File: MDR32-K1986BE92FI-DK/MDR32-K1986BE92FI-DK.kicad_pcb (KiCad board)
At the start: 2 copper layers, 57 parts, among them J1 Conn_PROBE, J2 PIN_A, J3 SYS_A, J4 USB_C_Receptacle_USB2.0_16P, J5 PIN_B, J6 SYS_B, Q1 AO3401A, SW1 IT-1181, SW2 SW_DIP_x02, SW3 IT-1181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

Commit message: start pcb sizes
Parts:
- moved J2 92.0 mm to (108.1, 47.5), turned to -90 degrees
- moved BT1 79.3 mm to (88.3, 95.2)
- moved C1 79.3 mm to (80.4, 105.0)
- moved C2 79.3 mm to (80.4, 108.0)
- moved C3 79.3 mm to (96.5, 105.1)
- moved D2 79.3 mm to (77.1, 115.2)
- moved D3 79.3 mm to (89.3, 131.3)
- moved D5 79.3 mm to (89.3, 134.4)
- moved F1 79.3 mm to (68.1, 88.2)
- moved F2 79.3 mm to (68.1, 90.7)
- moved J1 79.3 mm to (95.9, 121.8)
- moved J4 79.3 mm to (88.5, 114.8)
- moved JP1 79.3 mm to (84.9, 131.6)
- moved JP2 79.3 mm to (84.9, 135.1)
- moved R1 79.3 mm to (68.1, 93.2)
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
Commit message: change pinout on header
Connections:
- J2 pad 1: /PA0 -> GND
- J2 pad 10: /PB9 -> /PA6
- J2 pad 11: /PB8 -> /PA5
- J2 pad 12: /PB7 -> /PA4
- J2 pad 13: /PB6 -> /PA3
- J2 pad 14: /PB5 -> /PA2
- J2 pad 15: GND -> /PA1
- J2 pad 16: GND -> /PA0
- J2 pad 2: /PA1 -> GND
- J2 pad 3: /PA2 -> /PB5
- J2 pad 4: /PA3 -> /PB6
- J2 pad 5: /PA4 -> /PB7
- J2 pad 6: /PA5 -> /PB8
- J2 pad 7: /PA6 -> /PB9
- J2 pad 8: /PA7 -> /PB10
- J2 pad 9: /PB10 -> /PA7
- J3 pad 1: /JATDO -> GND
- J3 pad 10: GND -> /JATDO
- J3 pad 2: /JATMS -> +3V3_SRC
- J3 pad 3: /JATCK -> +BATT_SRC
- J3 pad 4: /JATDI -> /WAKEUP
- J3 pad 5: /JAnTRS -> /nRESET
- J3 pad 6: /nRESET -> /JAnTRS
- J3 pad 7: +BATT_SRC -> /JATDI
- J3 pad 8: +3V3_SRC -> /JATCK
- J3 pad 9: VUSB -> /JATMS
- J5 pad 1: /PC0 -> /PF0
- J5 pad 10: /PE3 -> /PE0
- J5 pad 11: /PE6 -> /PD7
- J5 pad 12: /PE7 -> /PD6
- J5 pad 13: /PF3 -> /PD5
- J5 pad 14: /PF2 -> /PC2
- J5 pad 15: /PF1 -> /PC1
- J5 pad 16: /PF0 -> /PC0
- J5 pad 2: /PC1 -> /PF1
- J5 pad 3: /PC2 -> /PF2
- J5 pad 4: /PD5 -> /PF3
- J5 pad 5: /PD6 -> /PE7
- J5 pad 6: /PD7 -> /PE6
- J5 pad 7: /PE0 -> /PE3
- J5 pad 8: /PE1 -> /PE2
- J5 pad 9: /PE2 -> /PE1
- J6 pad 1: /WAKEUP -> GND
- J6 pad 10: GND -> /JBTDO
- J6 pad 2: /JBTDO -> VUSB
- J6 pad 3: /JBTMS -> /PF4_MODE0
- J6 pad 4: /JBTCK -> /PF5_MODE1
- J6 pad 5: /JBTDI -> /PF6_MODE2
- J6 pad 7: /PF6_MODE2 -> /JBTDI
- J6 pad 8: /PF5_MODE1 -> /JBTCK
- J6 pad 9: /PF4_MODE0 -> /JBTMS
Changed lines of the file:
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@@
 		)
 		(fp_text user "${REFERENCE}"
-			(at 0 19.05 360)
+			(at 0 19.05 0)
 			(layer "F.Fab")
 			(effects
@@
 			(layers "*.Cu" "*.Mask")
 			(remove_unused_layers no)
-			(net 36 "/PC0")
+			(net 62 "/PF0")
 			(pinfunction "Pin_1")
 			(pintype "passive")
@@
 			(layers "*.Cu" "*.Mask")
 			(remove_unused_layers no)
-			(net 58 "/PC1")
+			(net 39 "/PF1")
 			(pinfunction "Pin_2")
 			(pintype "passive")
@@
 			(layers "*.Cu" "*.Mask")
 			(remove_unused_layers no)
-			(net 20 "/PC2")
+			(net 33 "/PF2")
 			(pinfunction "Pin_3")
 			(pintype "passive")
@@
 			(layers "*.Cu" "*.Mask")
 			(remove_unused_layers no)
-			(net 19 "/PD5")
+			(net 45 "/PF3")
 			(pinfunction "Pin_4")
 			(pintype "passive")
@@
 			(layers "*.Cu" "*.Mask")
 			(remove_unused_layers no)
-			(net 38 "/PD6")
+			(net 66 "/PE7")
 			(pinfunction "Pin_5")
 			(pintype "passive")
@@
 			(layers "*.Cu" "*.Mask")
 			(remove_unused_layers no)
-			(net 43 "/PD7")
+			(net 67 "/PE6")
 			(pinfunction "Pin_6")
 			(pintype "passive")
@@
 			(layers "*.Cu" "*.Mask")
 			(remove_unused_layers no)
-			(net 47 "/PE0")
+			(net 44 "/PE3")
 			(pinfunction "Pin_7")
 			(pintype "passive")
@@
 			(layers "*.Cu" "*.Mask")
 			(remove_unused_layers no)
-			(net 48 "/PE1")
+			(net 61 "/PE2")
 			(pinfunction "Pin_8")
 			(pintype "passive")
@@
 			(layers "*.Cu" "*.Mask")
 			(remove_unused_layers no)
-			(net 61 "/PE2")
+			(net 48 "/PE1")
 			(pinfunction "Pin_9")
 			(pintype "passive")
@@
 			(layers "*.Cu" "*.Mask")
 			(remove_unused_layers no)
-			(net 44 "/PE3")
+			(net 47 "/PE0")
 			(pinfunction "Pin_10")
 			(pintype "passive")
@@
 			(layers "*.Cu" "*.Mask")
 			(remove_unused_layers no)
-			(net 67 "/PE6")
+			(net 43 "/PD7")
 			(pinfunction "Pin_11")
 			(pintype "passive")
@@
 			(layers "*.Cu" "*.Mask")
 			(remove_unused_layers no)
-			(net 66 "/PE7")
+			(net 38 "/PD6")
 			(pinfunction "Pin_12")
 			(pintype "passive")
@@
 			(layers "*.Cu" "*.Mask")
 			(remove_unused_layers no)
-			(net 45 "/PF3")
+			(net 19 "/PD5")
 			(pinfunction "Pin_13")
 			(pintype "passive")
@@
 			(layers "*.Cu" "*.Mask")
 			(remove_unused_layers no)
-			(net 33 "/PF2")
+			(net 20 "/PC2")
 			(pinfunction "Pin_14")
 			(pintype "passive")
@@
 			(layers "*.Cu" "*.Mask")
 			(remove_unused_layers no)
-			(net 39 "/PF1")
+			(net 58 "/PC1")
 			(pinfunction "Pin_15")
 			(pintype "passive")
@@
 			(layers "*.Cu" "*.Mask")
 			(remove_unused_layers no)
-			(net 62 "/PF0")
+			(net 36 "/PC0")
 			(pinfunction "Pin_16")
 			(pintype "passive")
@@
 		)
 		(fp_text user "${REFERENCE}"
-			(at 0 11.43 360)
+			(at 0 11.43 0)
 			(layer "F.Fab")
 			(effects
@@
 			(layers "*.Cu" "*.Mask")
 			(remove_unused_layers no)
-			(net 8 "/WAKEUP")
+			(net 9 "GND")
 			(pinfunction "Pin_1")
 			(pintype "passive")
@@
 			(layers "*.Cu" "*.Mask")
 			(remove_unused_layers no)
-			(net 6 "/JBTDO")
+			(net 31 "VUSB")
 			(pinfunction "Pin_2")
 			(pintype "passive")
@@
 			(layers "*.Cu" "*.Mask")
 			(remove_unused_layers no)
-			(net 4 "/JBTMS")
+			(net 16 "/PF4_MODE0")
 			(pinfunction "Pin_3")
 			(pintype "passive")
@@
 			(layers "*.Cu" "*.Mask")
 			(remove_unused_layers no)
-			(net 5 "/JBTCK")
+			(net 17 "/PF5_MODE1")
 			(pinfunction "Pin_4")
 			(pintype "passive")
@@
 			(layers "*.Cu" "*.Mask")
 			(remove_unused_layers no)
-			(net 3 "/JBTDI")
+			(net 18 "/PF6_MODE2")
 			(pinfunction "Pin_5")
 			(pintype "passive")
@@
 			(layers "*.Cu" "*.Mask")
 			(remove_unused_layers no)
-			(net 18 "/PF6_MODE2")
+			(net 3 "/JBTDI")
 			(pinfunction "Pin_7")
 			(pintype "passive")
@@
 			(layers "*.Cu" "*.Mask")
 			(remove_unused_layers no)
-			(net 17 "/PF5_MODE1")
+			(net 5 "/JBTCK")
 			(pinfunction "Pin_8")
 			(pintype "passive")
@@
 			(layers "*.Cu" "*.Mask")
 			(remove_unused_layers no)
-			(net 16 "/PF4_MODE0")
+			(net 4 "/JBTMS")
 			(pinfunction "Pin_9")
 			(pintype "passive")
@@
 			(layers "*.Cu" "*.Mask")
 			(remove_unused_layers no)
-			(net 9 "GND")
+			(net 6 "/JBTDO")
 			(pinfunction "Pin_10")
 			(pintype "passive")
@@
 		)
 		(fp_text user "${REFERENCE}"
-			(at 0 19.05 360)
+			(at 0 19.05 0)
 			(layer "F.Fab")
 			(effects
@@
 			(layers "*.Cu" "*.Mask")
 			(remove_unused_layers no)
-			(net 60 "/PA0")
+			(net 9 "GND")
 			(pinfunction "Pin_1")
 			(pintype "passive")
@@
 			(layers "*.Cu" "*.Mask")
 			(remove_unused_layers no)
-			(net 52 "/PA1")
+			(net 9 "GND")
 			(pinfunction "Pin_2")
 			(pintype "passive")
@@
 			(layers "*.Cu" "*.Mask")
 			(remove_unused_layers no)
-			(net 35 "/PA2")
+			(net 59 "/PB5")
 			(pinfunction "Pin_3")
 			(pintype "passive")
@@
 			(layers "*.Cu" "*.Mask")
 			(remove_unused_layers no)
-			(net 37 "/PA3")
+			(net 63 "/PB6")
 			(pinfunction "Pin_4")
 			(pintype "passive")
@@
 			(layers "*.Cu" "*.Mask")
 			(remove_unused_layers no)
-			(net 46 "/PA4")
+			(net 55 "/PB7")
 			(pinfunction "Pin_5")
 			(pintype "passive")
@@
 			(layers "*.Cu" "*.Mask")
 			(remove_unused_layers no)
-			(net 56 "/PA5")
+			(net 41 "/PB8")
 			(pinfunction "Pin_6")
 			(pintype "passive")
@@
 			(layers "*.Cu" "*.Mask")
 			(remove_unused_layers no)
-			(net 53 "/PA6")
+			(net 57 "/PB9")
 			(pinfunction "Pin_7")
 			(pintype "passive")
@@
 			(layers "*.Cu" "*.Mask")
 			(remove_unused_layers no)
-			(net 49 "/PA7")
+			(net 40 "/PB10")
 			(pinfunction "Pin_8")
 			(pintype "passive")
@@
 			(layers "*.Cu" "*.Mask")
 			(remove_unused_layers no)
-			(net 40 "/PB10")
+			(net 49 "/PA7")
 			(pinfunction "Pin_9")
 			(pintype "passive")
@@
 			(layers "*.Cu" "*.Mask")
 			(remove_unused_layers no)
-			(net 57 "/PB9")
+			(net 53 "/PA6")
 			(pinfunction "Pin_10")
 			(pintype "passive")
@@
 			(layers "*.Cu" "*.Mask")
 			(remove_unused_layers no)
-			(net 41 "/PB8")
+			(net 56 "/PA5")
 			(pinfunction "Pin_11")
 			(pintype "passive")
@@
 			(layers "*.Cu" "*.Mask")
 			(remove_unused_layers no)
-			(net 55 "/PB7")
+			(net 46 "/PA4")
 			(pinfunction "Pin_12")
 			(pintype "passive")
@@
 			(layers "*.Cu" "*.Mask")
 			(remove_unused_layers no)
-			(net 63 "/PB6")
+			(net 37 "/PA3")
 			(pinfunction "Pin_13")
 			(pintype "passive")
@@
 			(layers "*.Cu" "*.Mask")
 			(remove_unused_layers no)
-			(net 59 "/PB5")
+			(net 35 "/PA2")
 			(pinfunction "Pin_14")
 			(pintype "passive")
@@
 			(layers "*.Cu" "*.Mask")
 			(remove_unused_layers no)
-			(net 9 "GND")
+			(net 52 "/PA1")
 			(pinfunction "Pin_15")
 			(pintype "passive")
@@
 			(layers "*.Cu" "*.Mask")
 			(remove_unused_layers no)
-			(net 9 "GND")
+			(net 60 "/PA0")
 			(pinfunction "Pin_16")
 			(pintype "passive")
@@
 		)
 		(fp_text user "${REFERENCE}"
-			(at 0 11.43 360)
+			(at 0 11.43 0)
 			(layer "F.Fab")
 			(effects
@@
 			(layers "*.Cu" "*.Mask")
 			(remove_unused_layers no)
-			(net 25 "/JATDO")
+			(net 9 "GND")
 			(pinfunction "Pin_1")
 			(pintype "passive")
@@
 			(layers "*.Cu" "*.Mask")
 			(remove_unused_layers no)
-			(net 13 "/JATMS")
+			(net 29 "+3V3_SRC")
 			(pinfunction "Pin_2")
 			(pintype "passive")
@@
 			(layers "*.Cu" "*.Mask")
 			(remove_unused_layers no)
-			(net 14 "/JATCK")
+			(net 27 "+BATT_SRC")
 			(pinfunction "Pin_3")
 			(pintype "passive")
@@
 			(layers "*.Cu" "*.Mask")
 			(remove_unused_layers no)
-			(net 12 "/JATDI")
+			(net 8 "/WAKEUP")
 			(pinfunction "Pin_4")
 			(pintype "passive")
@@
 			(layers "*.Cu" "*.Mask")
 			(remove_unused_layers no)
-			(net 2 "/JAnTRS")
+			(net 15 "/nRESET")
 			(pinfunction "Pin_5")
 			(pintype "passive")
@@
 			(layers "*.Cu" "*.Mask")
 			(remove_unused_layers no)
-			(net 15 "/nRESET")
+			(net 2 "/JAnTRS")
 			(pinfunction "Pin_6")
 			(pintype "passive")
@@
 			(layers "*.Cu" "*.Mask")
 			(remove_unused_layers no)
-			(net 27 "+BATT_SRC")
+			(net 12 "/JATDI")
 			(pinfunction "Pin_7")
 			(pintype "passive")
@@
 			(layers "*.Cu" "*.Mask")
 			(remove_unused_layers no)
-			(net 29 "+3V3_SRC")
+			(net 14 "/JATCK")
 			(pinfunction "Pin_8")
 			(pintype "passive")
@@
 			(layers "*.Cu" "*.Mask")
 			(remove_unused_layers no)
-			(net 31 "VUSB")
+			(net 13 "/JATMS")
 			(pinfunction "Pin_9")
 			(pintype "passive")
@@
 			(layers "*.Cu" "*.Mask")
 			(remove_unused_layers no)
-			(net 9 "GND")
+			(net 25 "/JATDO")
 			(pinfunction "Pin_10")
 			(pintype "passive")

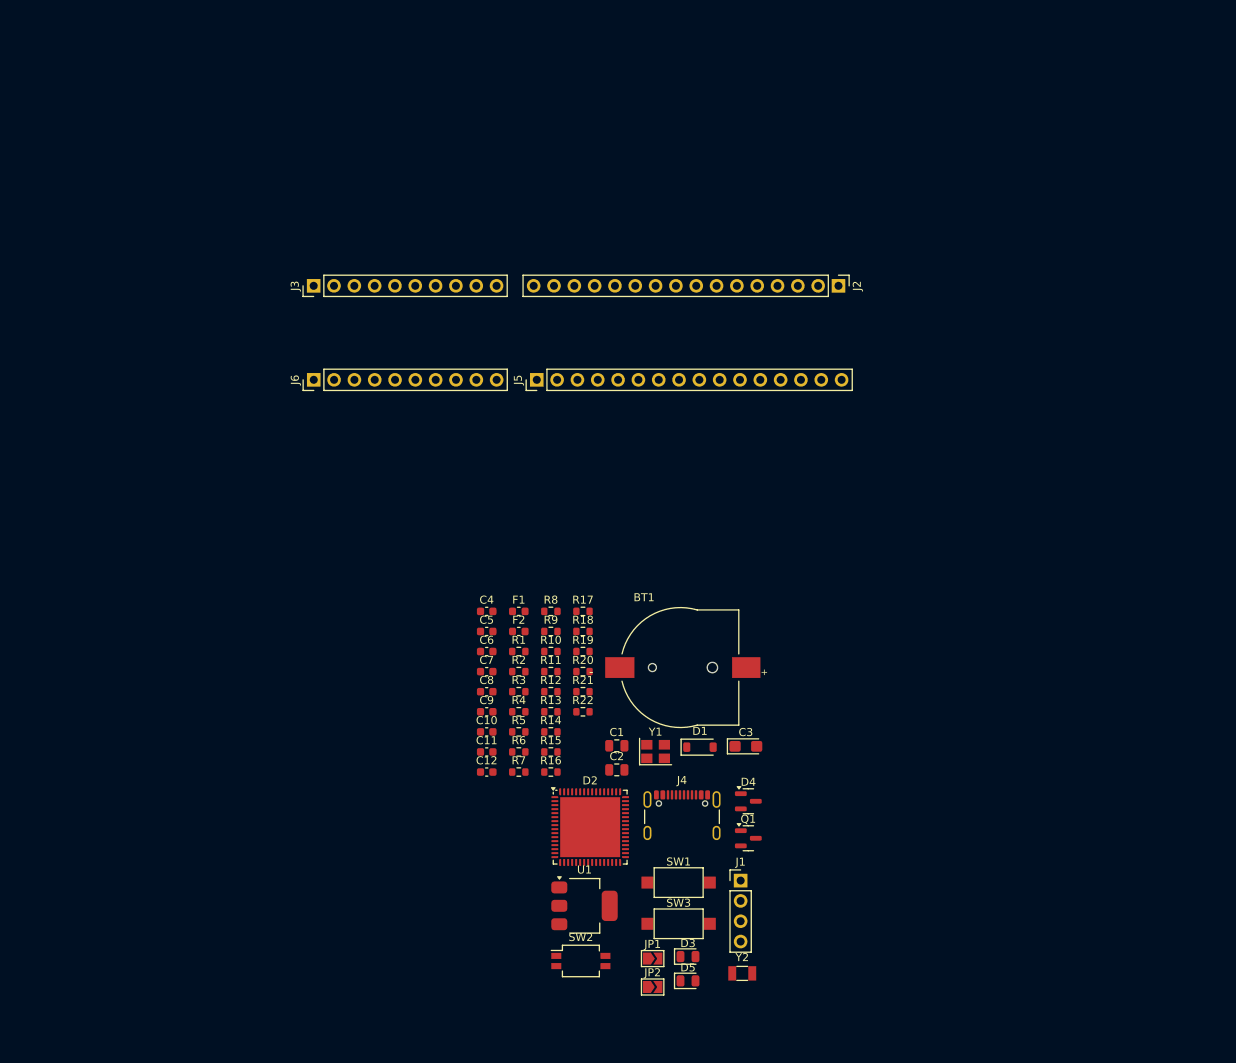
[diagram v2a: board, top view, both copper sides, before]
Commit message: position and sizes
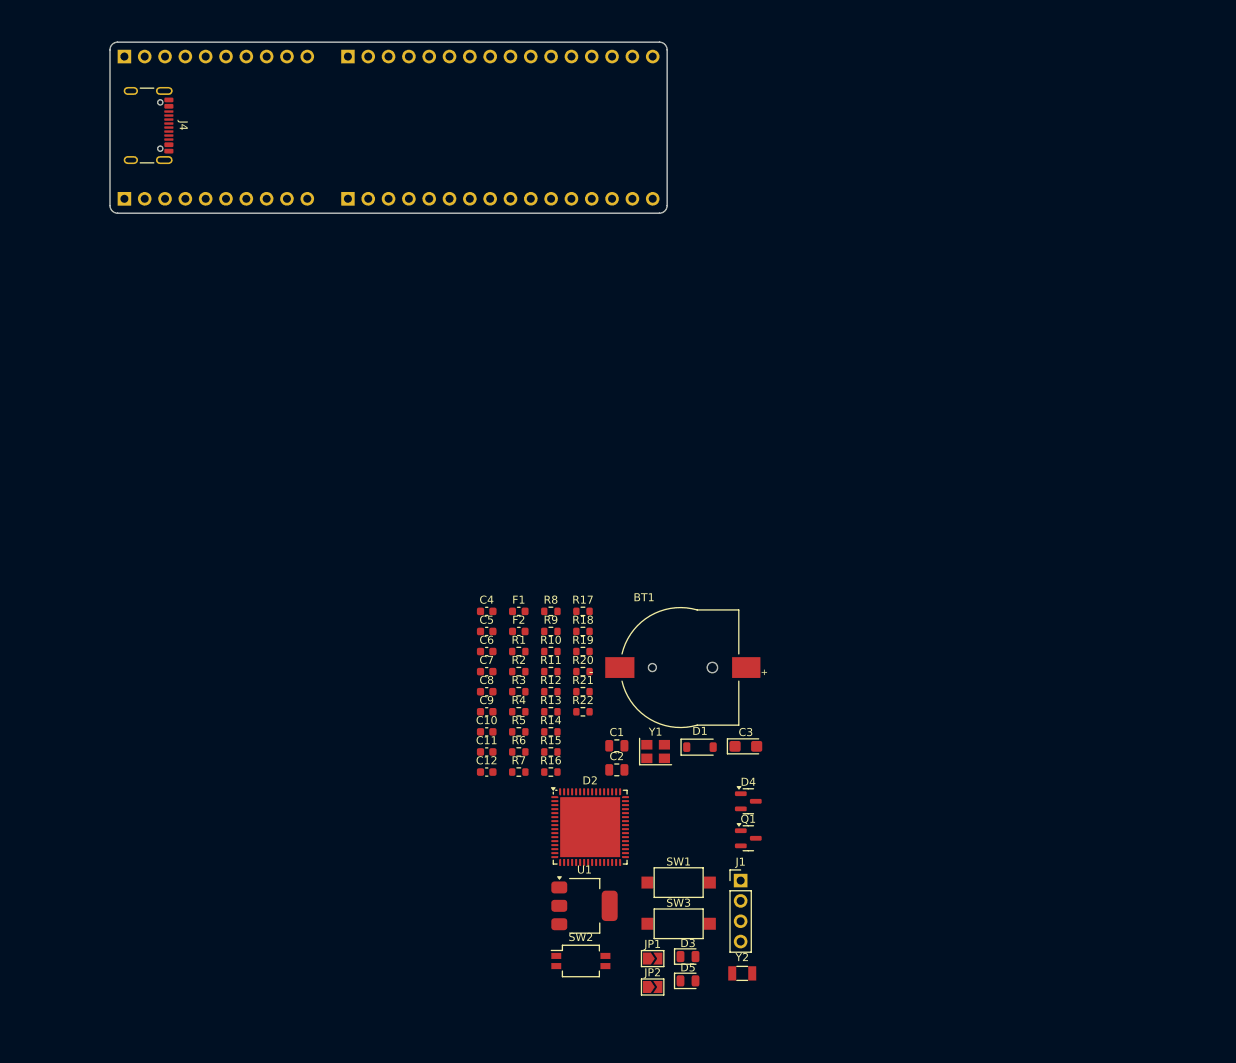
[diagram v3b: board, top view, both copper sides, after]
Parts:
- J2, J3, J5, J6: moved to B.Cu
- moved J4 110.6 mm to (20.7, 27.5), turned to -90 degrees
- moved J2 62.3 mm to (46.8, 36.6)
- moved J6 46.8 mm to (18.8, 18.8), turned to -90 degrees
- moved J5 46.8 mm to (46.8, 18.8), turned to -90 degrees
- moved J3 26.0 mm to (18.8, 36.6), turned to -90 degrees
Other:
- board outline added: 69.6 x 21.4 mm

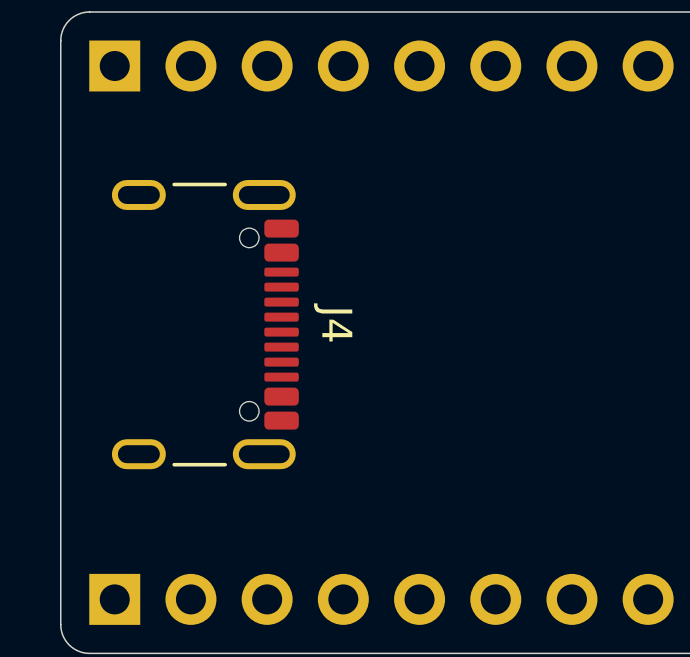
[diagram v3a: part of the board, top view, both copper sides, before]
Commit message: usb position on pcb
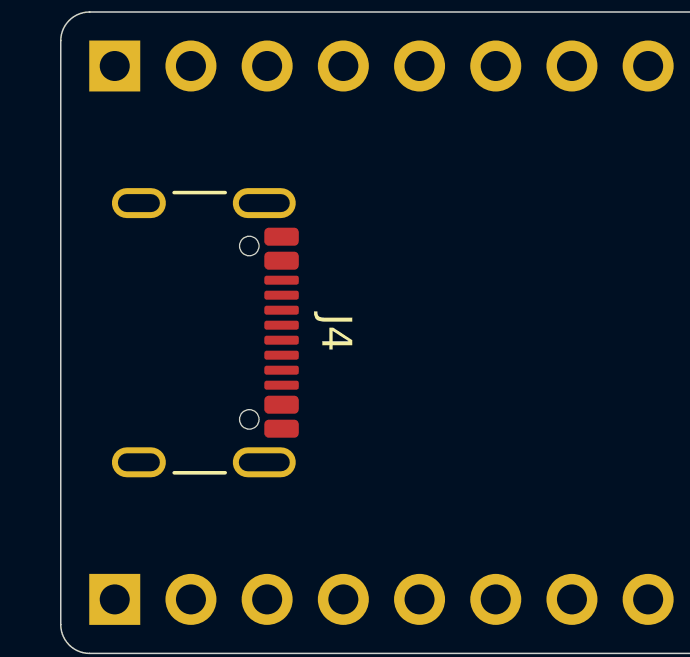
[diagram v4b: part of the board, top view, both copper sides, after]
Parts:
- moved J4 0.27 mm to (20.7, 27.7)
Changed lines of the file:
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@@
 	)
 	(footprint "Connector_USB:USB_C_Receptacle_GCT_USB4105-xx-A_16P_TopMnt_Horizontal"
+		(locked yes)
 		(layer "F.Cu")
-		(at 20.72 27.46 -90)
+		(at 20.72 27.73 -90)
 		(descr "USB 2.0 Type C Receptacle, GCT, 16P, top mounted, horizontal, 5A: https://gct.co/files/drawings/usb4105.pdf")
 		(tags "USB C Type-C Receptacle SMD USB 2.0 16P 16C USB4105-15-A USB4105-15-A-060 USB4105-15-A-120 USB4105-GF-A USB4105-GF-A-060 USB4105-GF-A-120")
@@
 	)
 	(footprint "Connector_PinHeader_2.54mm:PinHeader_1x16_P2.54mm_Vertical"
+		(locked yes)
 		(layer "B.Cu")
 		(at 46.78 18.84 -90)
@@
 		)
 		(fp_text user "${REFERENCE}"
-			(at 0 -19.05 360)
+			(at 0 -19.05 0)
 			(layer "B.Fab")
 			(effects
@@
 	)
 	(footprint "Connector_PinHeader_2.54mm:PinHeader_1x10_P2.54mm_Vertical"
+		(locked yes)
 		(layer "B.Cu")
 		(at 18.84 18.84 -90)
@@
 		)
 		(fp_text user "${REFERENCE}"
-			(at 0 -11.43 360)
+			(at 0 -11.43 0)
 			(layer "B.Fab")
 			(effects
@@
 	)
 	(footprint "Connector_PinHeader_2.54mm:PinHeader_1x16_P2.54mm_Vertical"
+		(locked yes)
 		(layer "B.Cu")
 		(at 46.78 36.62 -90)
@@
 		)
 		(fp_text user "${REFERENCE}"
-			(at 0 -19.05 360)
+			(at 0 -19.05 0)
 			(layer "B.Fab")
 			(effects
@@
 	)
 	(footprint "Connector_PinHeader_2.54mm:PinHeader_1x10_P2.54mm_Vertical"
+		(locked yes)
 		(layer "B.Cu")
 		(at 18.84 36.62 -90)
@@
 		)
 		(fp_text user "${REFERENCE}"
-			(at 0 -11.43 360)
+			(at 0 -11.43 0)
 			(layer "B.Fab")
 			(effects
@@
 		(start 86.68 37.46)
 		(end 86.68 18)
+		(locked yes)
 		(stroke
 			(width 0.05)
@@
 		(mid 86.398823 17.321177)
 		(end 86.68 18)
+		(locked yes)
 		(stroke
 			(width 0.05)
@@
 		(mid 86.398823 38.138823)
 		(end 85.72 38.42)
+		(locked yes)
 		(stroke
 			(width 0.05)
@@
 		(start 18 17.04)
 		(end 85.72 17.04)
+		(locked yes)
 		(stroke
 			(width 0.05)
@@
 		(mid 17.321177 38.138823)
 		(end 17.04 37.46)
+		(locked yes)
 		(stroke
 			(width 0.05)
@@
 		(mid 17.321177 17.321177)
 		(end 18 17.04)
+		(locked yes)
 		(stroke
 			(width 0.05)
@@
 		(start 17.04 18)
 		(end 17.04 37.46)
+		(locked yes)
 		(stroke
 			(width 0.05)
@@
 		(start 18 38.42)
 		(end 85.72 38.42)
+		(locked yes)
 		(stroke
 			(width 0.05)
@@
 	(dimension
 		(type aligned)
+		(locked yes)
 		(layer "Dwgs.User")
 		(pts
@@
 		(height -69.64)
 		(gr_text "21,3800 mm"
+			(locked yes)
 			(at 87.89 27.73 90)
 			(layer "Dwgs.User")
@@
 	(dimension
 		(type aligned)
+		(locked yes)
 		(layer "Dwgs.User")
 		(pts
@@
 		(height 21.38)
 		(gr_text "69,6400 mm"
+			(locked yes)
 			(at 51.85 39.63 0)
 			(layer "Dwgs.User")
